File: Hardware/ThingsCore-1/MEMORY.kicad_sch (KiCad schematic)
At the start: 27 parts, among them U10 EMMC04G-M627-A01, U8 W25Q256JVEIQ, U9 TF-123B-ARP9H17

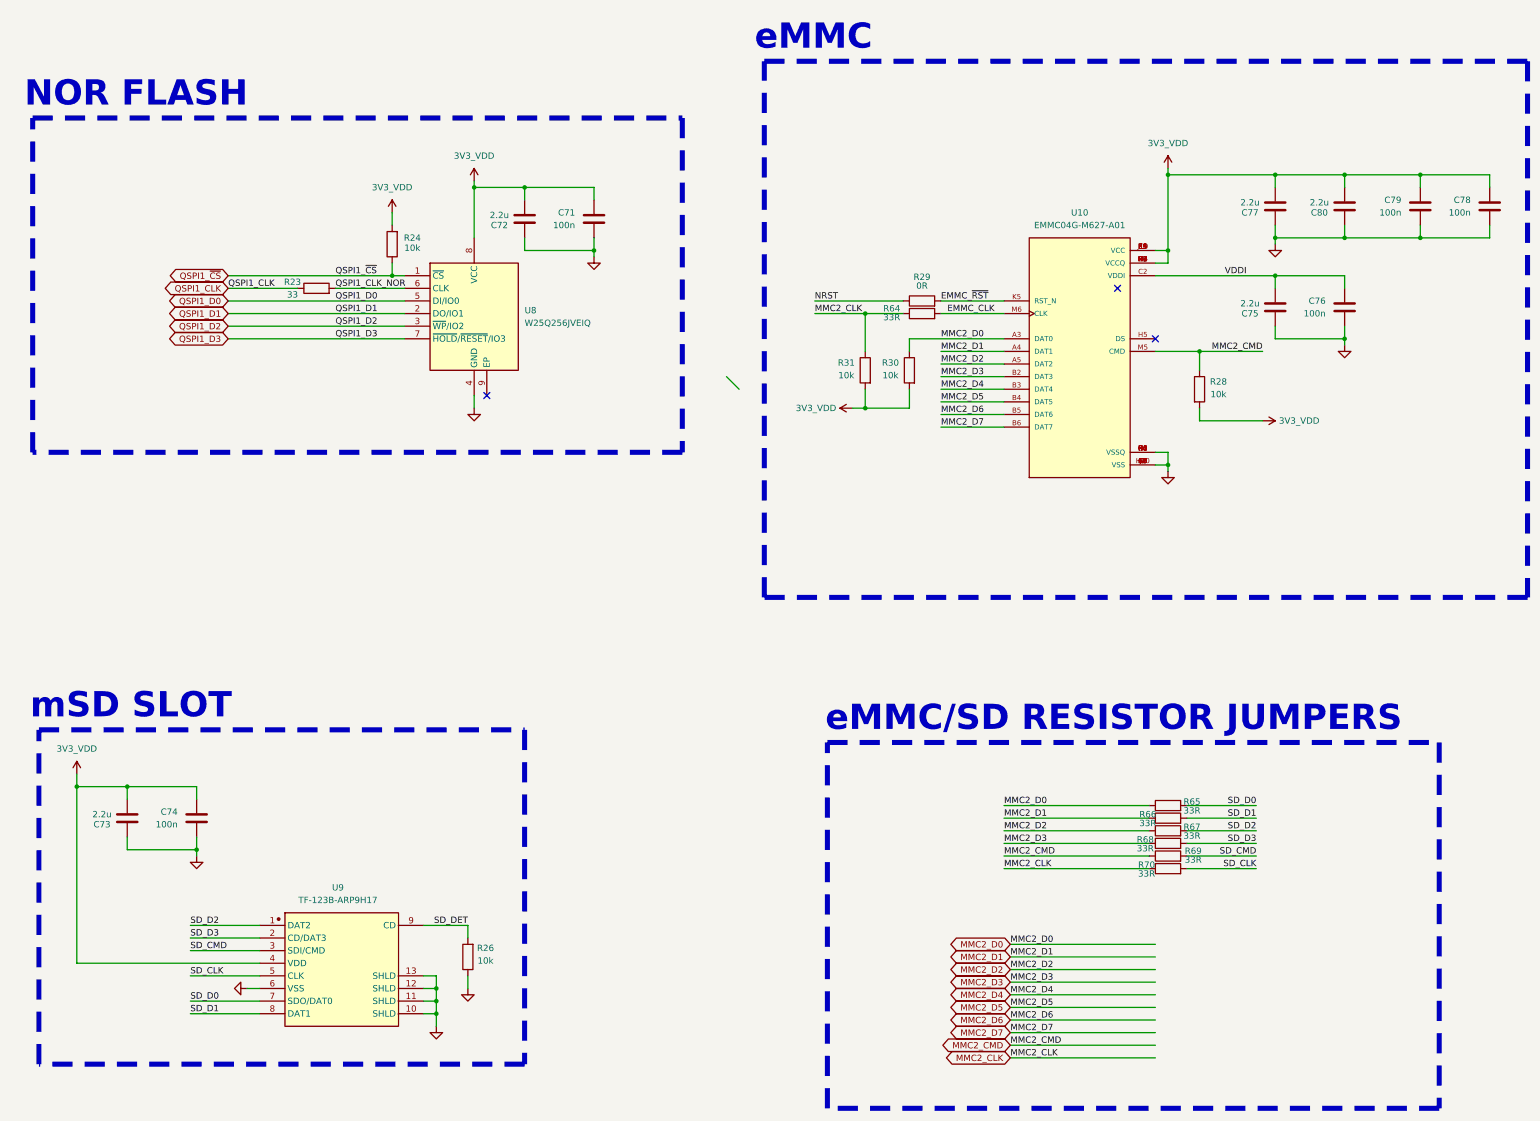
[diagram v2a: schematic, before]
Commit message: checks left and feedback resistors for switchers
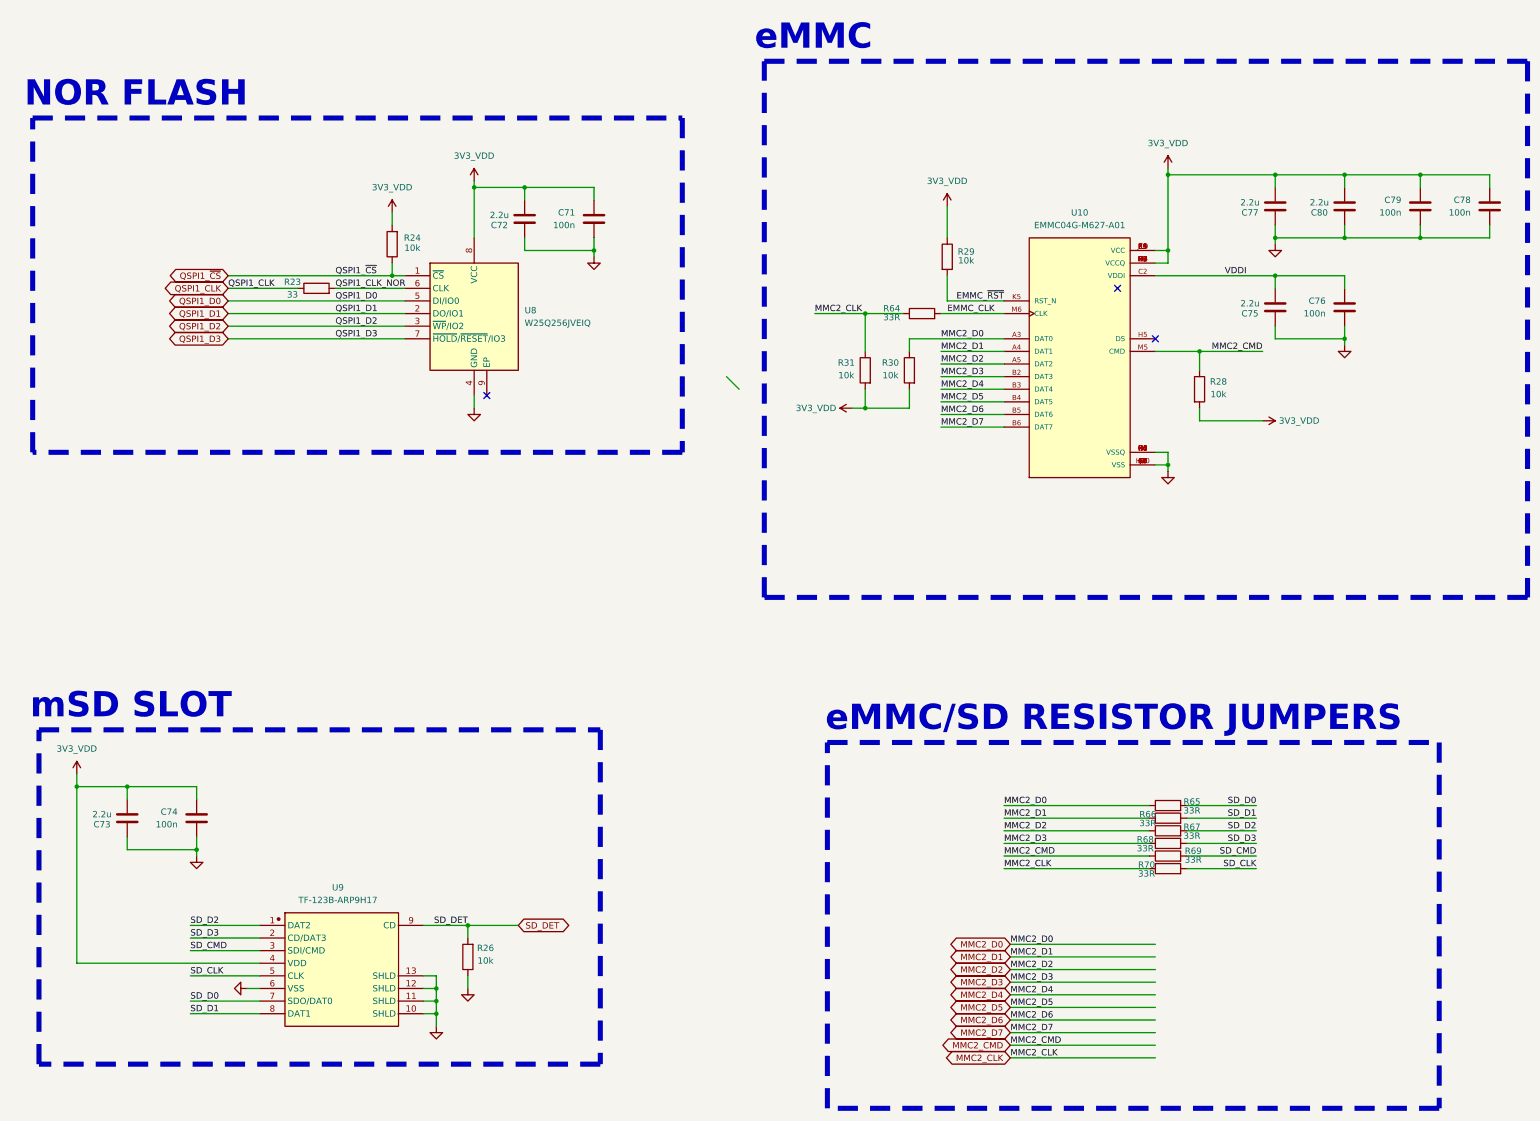
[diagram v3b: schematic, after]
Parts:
- R29: value 0R -> 10k
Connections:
- net NRST is gone; now on net 3V3_VDD: R29.1
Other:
- moved on the sheet: R29
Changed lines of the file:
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@@
 	(rectangle
 		(start 72.39 171.45)
-		(end 170.18 238.76)
+		(end 185.42 238.76)
 		(stroke
 			(width 1.016)
@@
 	)
 	(junction
+		(at 158.75 210.82)
+		(diameter 0)
+		(color 0 0 0 0)
+	)
+	(junction
 		(at 335.28 92.71)
 		(diameter 0)
@@
 	(wire
 		(pts
+			(xy 158.75 210.82) (xy 158.75 213.36)
+		)
+		(stroke
+			(width 0)
+			(type default)
+		)
+	)
+	(wire
+		(pts
 			(xy 254 100.33) (xy 266.7 100.33)
 		)
@@
 	(wire
 		(pts
+			(xy 158.75 210.82) (xy 168.91 210.82)
+		)
+		(stroke
+			(width 0)
+			(type default)
+		)
+	)
+	(wire
+		(pts
 			(xy 238.76 87.63) (xy 246.38 87.63)
 		)
@@
 	(wire
 		(pts
+			(xy 266.7 85.09) (xy 255.27 85.09)
+		)
+		(stroke
+			(width 0)
+			(type default)
+		)
+	)
+	(wire
+		(pts
 			(xy 102.87 210.82) (xy 116.84 210.82)
 		)
@@
 	(wire
 		(pts
-			(xy 335.28 59.69) (xy 350.52 59.69)
+			(xy 255.27 85.09) (xy 255.27 80.01)
 		)
 		(stroke
@@
 	(wire
 		(pts
-			(xy 238.76 106.68) (xy 236.22 106.68)
+			(xy 335.28 59.69) (xy 350.52 59.69)
 		)
 		(stroke
@@
 	(wire
 		(pts
-			(xy 90.17 182.88) (xy 90.17 185.42)
+			(xy 238.76 106.68) (xy 236.22 106.68)
 		)
 		(stroke
@@
 	(wire
 		(pts
-			(xy 158.75 210.82) (xy 158.75 213.36)
+			(xy 90.17 182.88) (xy 90.17 185.42)
 		)
 		(stroke
@@
 	(wire
 		(pts
-			(xy 228.6 85.09) (xy 246.38 85.09)
-		)
-		(stroke
-			(width 0)
-			(type default)
-		)
-	)
-	(wire
-		(pts
 			(xy 299.72 77.47) (xy 299.72 74.93)
 		)
@@
 	(wire
 		(pts
-			(xy 254 85.09) (xy 266.7 85.09)
+			(xy 132.08 82.55) (xy 146.05 82.55)
 		)
 		(stroke
@@
 	(wire
 		(pts
-			(xy 132.08 82.55) (xy 146.05 82.55)
+			(xy 149.86 228.6) (xy 152.4 228.6)
 		)
 		(stroke
@@
 	(wire
 		(pts
-			(xy 149.86 228.6) (xy 152.4 228.6)
+			(xy 335.28 93.98) (xy 335.28 92.71)
 		)
 		(stroke
@@
 	(wire
 		(pts
-			(xy 335.28 93.98) (xy 335.28 92.71)
+			(xy 254 107.95) (xy 266.7 107.95)
 		)
 		(stroke
@@
 	(wire
 		(pts
-			(xy 254 107.95) (xy 266.7 107.95)
+			(xy 267.97 234.95) (xy 297.18 234.95)
 		)
 		(stroke
@@
 	(wire
 		(pts
-			(xy 267.97 234.95) (xy 297.18 234.95)
+			(xy 255.27 66.04) (xy 255.27 72.39)
 		)
 		(stroke
@@
 	)
 	(label "EMMC_~{RST}"
-		(at 254 85.09 0)
+		(at 266.7 85.09 180)
 		(effects
 			(font
 				(size 1.27 1.27)
 			)
-			(justify left bottom)
+			(justify right bottom)
 		)
 	)
@@
 		)
 	)
-	(label "NRST"
-		(at 228.6 85.09 0)
-		(effects
-			(font
-				(size 1.27 1.27)
-			)
-			(justify left bottom)
-		)
-	)
 	(label "MMC2_CMD"
 		(at 267.97 234.95 0)
@@
 		)
 	)
+	(global_label "SD_DET"
+		(shape bidirectional)
+		(at 168.91 210.82 0)
+		(fields_autoplaced yes)
+		(effects
+			(font
+				(size 1.27 1.27)
+			)
+			(justify left)
+		)
+		(property "Intersheetrefs" "${INTERSHEET_REFS}"
+			(at 179.8402 210.82 0)
+			(effects
+				(font
+					(size 1.27 1.27)
+				)
+				(justify left)
+				(hide yes)
+			)
+		)
+	)
 	(global_label "MMC2_CMD"
 		(shape bidirectional)
@@
 	(symbol
 		(lib_id "Device:R")
-		(at 250.19 85.09 90)
+		(at 255.27 76.2 0)
 		(unit 1)
 		(exclude_from_sim no)
@@
 		(dnp no)
 		(property "Reference" "R29"
-			(at 250.19 80.264 90)
+			(at 259.08 75.184 0)
 			(effects
 				(font
@@
 			)
 		)
-		(property "Value" "0R"
-			(at 250.19 82.042 90)
+		(property "Value" "10k"
+			(at 259.08 76.962 0)
 			(effects
 				(font
@@
 		)
 		(property "Footprint" "Resistor_SMD:R_0402_1005Metric"
-			(at 250.19 86.868 90)
+			(at 253.492 76.2 90)
 			(effects
 				(font
@@
 		)
 		(property "Datasheet" "~"
-			(at 250.19 85.09 0)
+			(at 255.27 76.2 0)
 			(effects
 				(font
@@
 		)
 		(property "Description" "Resistor"
-			(at 250.19 85.09 0)
+			(at 255.27 76.2 0)
 			(effects
 				(font
@@
 					(unit 1)
 				)
+			)
+		)
+	)
+	(symbol
+		(lib_id "power:+1V0")
+		(at 255.27 66.04 0)
+		(unit 1)
+		(exclude_from_sim no)
+		(in_bom yes)
+		(on_board yes)
+		(dnp no)
+		(property "Reference" "#PWR0137"
+			(at 255.27 69.85 0)
+			(effects
+				(font
+					(size 1.27 1.27)
+				)
+				(hide yes)
+			)
+		)
+		(property "Value" "3V3_VDD"
+			(at 255.27 60.96 0)
+			(effects
+				(font
+					(size 1.27 1.27)
+				)
+			)
+		)
+		(property "Footprint" ""
+			(at 255.27 66.04 0)
+			(effects
+				(font
+					(size 1.27 1.27)
+				)
+				(hide yes)
+			)
+		)
+		(property "Datasheet" ""
+			(at 255.27 66.04 0)
+			(effects
+				(font
+					(size 1.27 1.27)
+				)
+				(hide yes)
+			)
+		)
+		(property "Description" "Power symbol creates a global label with name \"+1V0\""
+			(at 255.27 66.04 0)
+			(effects
+				(font
+					(size 1.27 1.27)
+				)
+				(hide yes)
+			)
+		)
+		(pin "1"
+		)
+		(instances
+			(project "ThingsCore-1"
+				(path "/0e14d4aa-2dd0-4b28-ae35-43afd1798b30/d807da36-b407-4754-85a6-ddc433365c5d"
+					(reference "#PWR0137")
+					(unit 1)
+				)
